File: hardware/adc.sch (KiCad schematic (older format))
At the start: 36 parts, among them U39 LP5907-3.0, U8 LTC2292

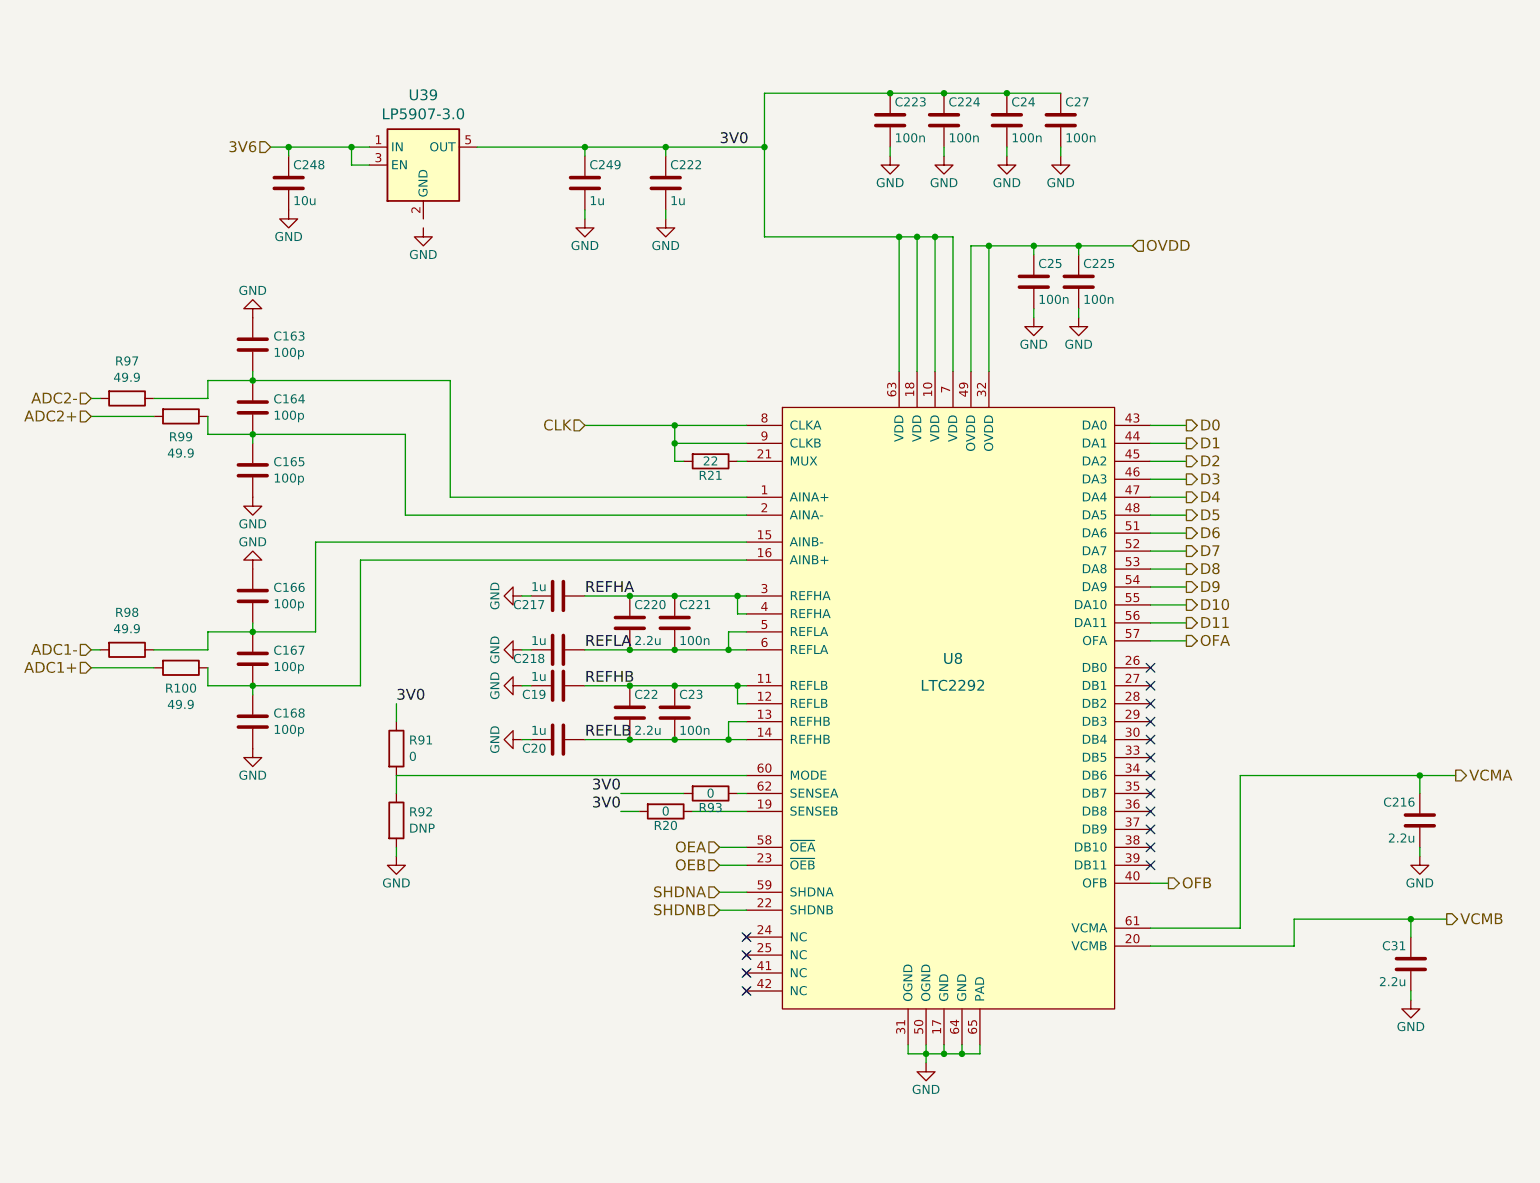
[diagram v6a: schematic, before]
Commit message: Improved documentation and parts of the schematic.
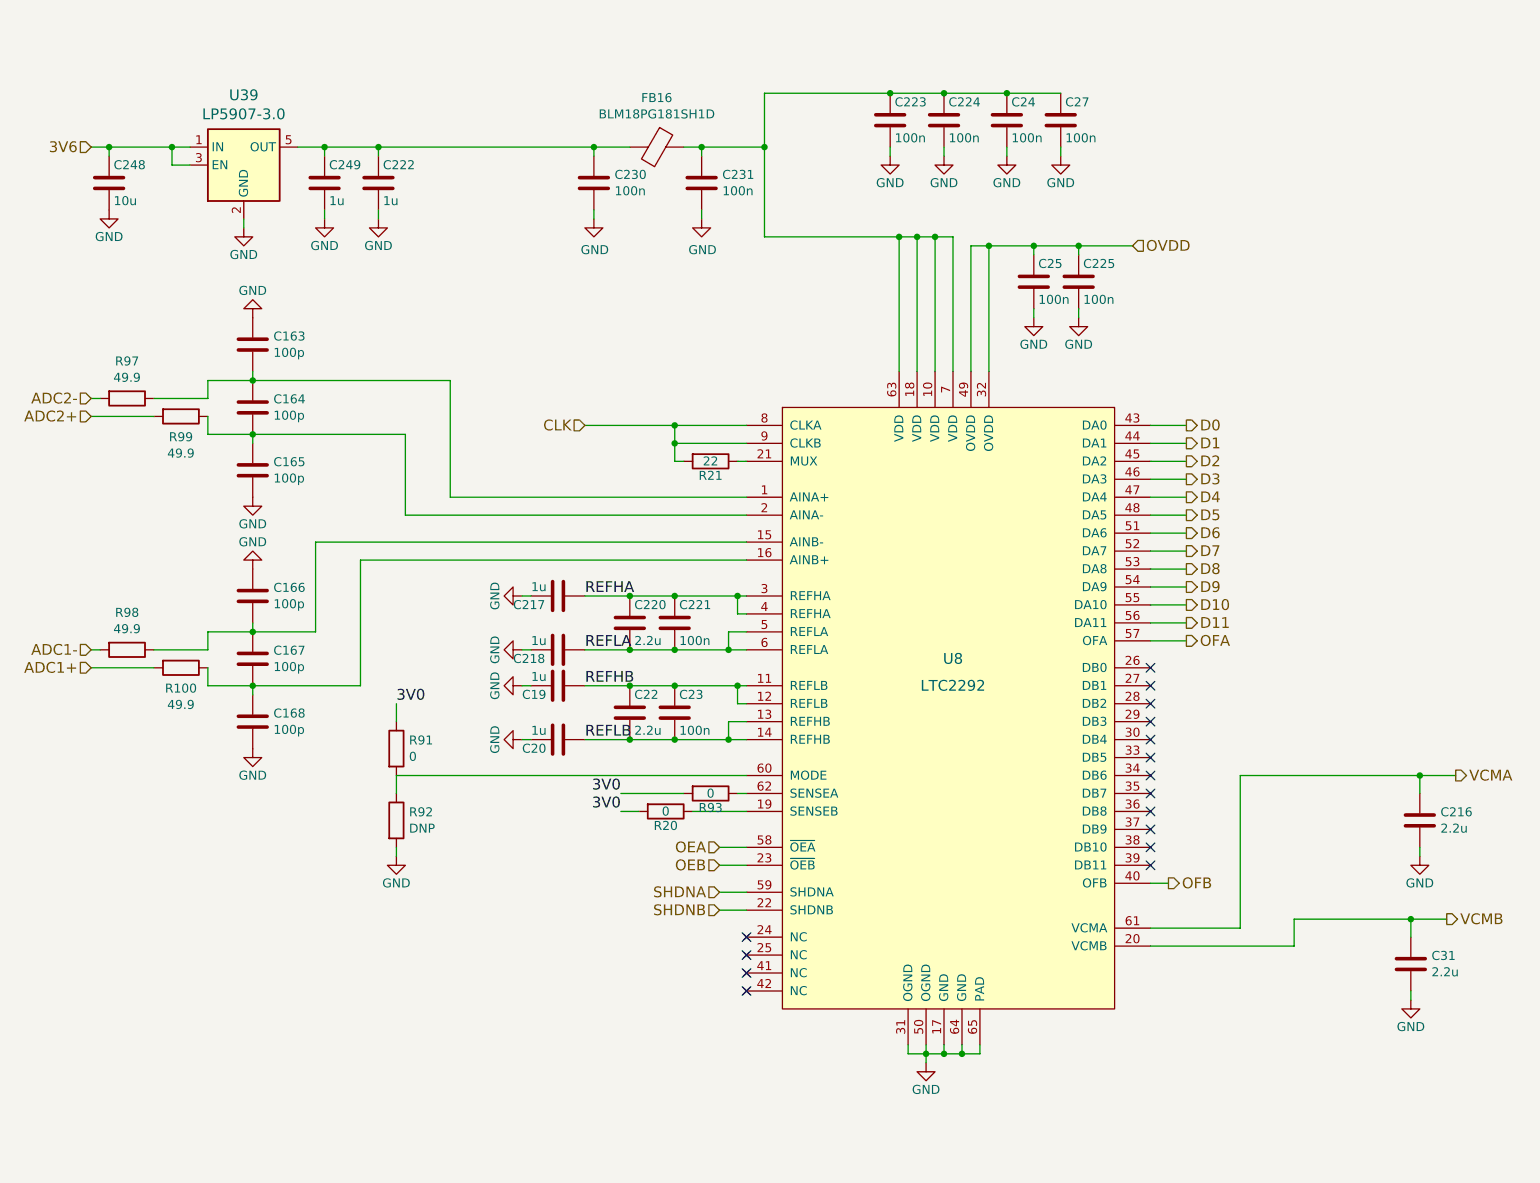
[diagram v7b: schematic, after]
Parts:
- added C230, C231: 100n, Capacitor_SMD:C_0402_1005Metric, symbol Device:C
- added FB16: BLM18PG181SH1D, Inductor_SMD:L_0603_1608Metric, symbol Device:Ferrite_Bead
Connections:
- net 3V0: no longer C222.1, C223.1, C224.1, C24.1, C249.1, C27.1, U39.5 (OUT), U8.10 (VDD), U8.18 (VDD), U8.63 (VDD), U8.7 (VDD)
- net GND: now also U39.2 (GND), C230.2, C231.2
- new net: C223.1, C224.1, C231.1, C24.1, C27.1, FB16.1, U8.10 (VDD), U8.18 (VDD), U8.63 (VDD), U8.7 (VDD)
- new net: C222.1, C230.1, C249.1, FB16.2, U39.5 (OUT)
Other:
- moved on the sheet: C222, C248, C249, U39
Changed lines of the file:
@@
 L Device:C C222
 U 1 1 583E443A
-P 4350 1550
-F 0 "C222" H 4375 1650 50  0000 L CNN
-F 1 "1u" H 4375 1450 50  0000 L CNN
-F 2 "Capacitor_SMD:C_0603_1608Metric" H 4388 1400 30  0001 C CNN
-F 3 "" H 4350 1550 60  0000 C CNN
-F 4 "CL10B105MO8NNWC" H 0   0   50  0001 C CNN "MFN"
-	1    4350 1550
+P 2750 1550
+F 0 "C222" H 2775 1650 50  0000 L CNN
+F 1 "1u" H 2775 1450 50  0000 L CNN
+F 2 "Capacitor_SMD:C_0603_1608Metric" H 2788 1400 30  0001 C CNN
+F 3 "" H 2750 1550 60  0000 C CNN
+F 4 "CL10B105MO8NNWC" H -1600 0   50  0001 C CNN "MFN"
+	1    2750 1550
 	1    0    0    -1
 $EndComp
@@
 L power:GND #PWR061
 U 1 1 583E44F5
-P 4350 1750
-F 0 "#PWR061" H 4350 1500 50  0001 C CNN
-F 1 "GND" H 4350 1600 50  0000 C CNN
-F 2 "" H 4350 1750 60  0000 C CNN
-F 3 "" H 4350 1750 60  0000 C CNN
-	1    4350 1750
+P 2750 1750
+F 0 "#PWR061" H 2750 1500 50  0001 C CNN
+F 1 "GND" H 2750 1600 50  0000 C CNN
+F 2 "" H 2750 1750 60  0000 C CNN
+F 3 "" H 2750 1750 60  0000 C CNN
+	1    2750 1750
 	1    0    0    -1
 $EndComp
@@
 U 1 1 583E8D35
 P 8550 5100
-F 0 "C216" H 8575 5200 50  0000 L CNN
-F 1 "2.2u" H 8575 5000 50  0000 L CNN
+F 0 "C216" H 8435 5146 50  0000 R CNN
+F 1 "2.2u" H 8435 5055 50  0000 R CNN
 F 2 "Capacitor_SMD:C_0603_1608Metric" H 8588 4950 30  0001 C CNN
 F 3 "" H 8550 5100 60  0000 C CNN
@@
 Text Label 2850 4450 0    60   ~ 0
 3V0
-Text Label 4650 1350 0    60   ~ 0
-3V0
 Text HLabel 7250 4100 2    60   Output ~ 0
 OFA
@@
 	2900 3400 4800 3400
 Wire Wire Line
-	3300 1350 3900 1350
-Wire Wire Line
-	4900 1050 4900 1350
-Wire Wire Line
-	4350 1400 4350 1350
-Connection ~ 4350 1350
-Wire Wire Line
-	4350 1700 4350 1750
+	2300 1350 2450 1350
+Wire Wire Line
+	2750 1400 2750 1350
+Wire Wire Line
+	2750 1700 2750 1750
 Wire Wire Line
 	5900 1350 5900 1400
@@
 L Regulator_Linear:LP5907MFX-3.0 U39
 U 1 1 58526584
-P 3000 1450
-F 0 "U39" H 3000 1839 60  0000 C CNN
-F 1 "LP5907-3.0" H 3000 1733 60  0000 C CNN
-F 2 "Package_TO_SOT_SMD:SOT-23-5" H 3000 1500 60  0001 C CNN
-F 3 "" H 3000 1500 60  0000 C CNN
-F 4 "LP5907MFX-3.0/NOPB" H 200 50  50  0001 C CNN "MFN"
-	1    3000 1450
+P 2000 1450
+F 0 "U39" H 2000 1839 60  0000 C CNN
+F 1 "LP5907-3.0" H 2000 1733 60  0000 C CNN
+F 2 "Package_TO_SOT_SMD:SOT-23-5" H 2000 1500 60  0001 C CNN
+F 3 "" H 2000 1500 60  0000 C CNN
+F 4 "LP5907MFX-3.0/NOPB" H -800 50  50  0001 C CNN "MFN"
+	1    2000 1450
 	1    0    0    -1
 $EndComp
@@
 L power:GND #PWR071
 U 1 1 585266D4
-P 3000 1800
-F 0 "#PWR071" H 3000 1550 50  0001 C CNN
-F 1 "GND" H 3000 1650 50  0000 C CNN
-F 2 "" H 3000 1800 60  0000 C CNN
-F 3 "" H 3000 1800 60  0000 C CNN
-	1    3000 1800
-	1    0    0    -1
-$EndComp
-Wire Wire Line
-	2700 1450 2600 1450
-Wire Wire Line
-	2600 1450 2600 1350
-Wire Wire Line
-	2150 1350 2250 1350
+P 2000 1800
+F 0 "#PWR071" H 2000 1550 50  0001 C CNN
+F 1 "GND" H 2000 1650 50  0000 C CNN
+F 2 "" H 2000 1800 60  0000 C CNN
+F 3 "" H 2000 1800 60  0000 C CNN
+	1    2000 1800
+	1    0    0    -1
+$EndComp
+Wire Wire Line
+	1700 1450 1600 1450
+Wire Wire Line
+	1600 1450 1600 1350
+Wire Wire Line
+	1150 1350 1250 1350
 $Comp
 L Device:C C248
 U 1 1 5852675F
-P 2250 1550
-F 0 "C248" H 2275 1650 50  0000 L CNN
-F 1 "10u" H 2275 1450 50  0000 L CNN
-F 2 "Capacitor_SMD:C_0805_2012Metric" H 2288 1400 30  0001 C CNN
-F 3 "" H 2250 1550 60  0000 C CNN
-F 4 "CL21B106KQQNNNE" H 400 0   50  0001 C CNN "MFN"
-	1    2250 1550
+P 1250 1550
+F 0 "C248" H 1275 1650 50  0000 L CNN
+F 1 "10u" H 1275 1450 50  0000 L CNN
+F 2 "Capacitor_SMD:C_0805_2012Metric" H 1288 1400 30  0001 C CNN
+F 3 "" H 1250 1550 60  0000 C CNN
+F 4 "CL21B106KQQNNNE" H -600 0   50  0001 C CNN "MFN"
+	1    1250 1550
 	1    0    0    -1
 $EndComp
@@
 L power:GND #PWR072
 U 1 1 585267C4
-P 2250 1700
-F 0 "#PWR072" H 2250 1450 50  0001 C CNN
-F 1 "GND" H 2250 1550 50  0000 C CNN
-F 2 "" H 2250 1700 60  0000 C CNN
-F 3 "" H 2250 1700 60  0000 C CNN
-	1    2250 1700
-	1    0    0    -1
-$EndComp
-Wire Wire Line
-	2250 1400 2250 1350
-Connection ~ 2600 1350
-Connection ~ 2250 1350
-Text HLabel 2150 1350 0    60   Input ~ 0
+P 1250 1700
+F 0 "#PWR072" H 1250 1450 50  0001 C CNN
+F 1 "GND" H 1250 1550 50  0000 C CNN
+F 2 "" H 1250 1700 60  0000 C CNN
+F 3 "" H 1250 1700 60  0000 C CNN
+	1    1250 1700
+	1    0    0    -1
+$EndComp
+Wire Wire Line
+	1250 1400 1250 1350
+Connection ~ 1600 1350
+Connection ~ 1250 1350
+Text HLabel 1150 1350 0    60   Input ~ 0
 3V6
 $Comp
 L Device:C C249
 U 1 1 585275B5
-P 3900 1550
-F 0 "C249" H 3925 1650 50  0000 L CNN
-F 1 "1u" H 3925 1450 50  0000 L CNN
-F 2 "Capacitor_SMD:C_0603_1608Metric" H 3938 1400 30  0001 C CNN
-F 3 "" H 3900 1550 60  0000 C CNN
-F 4 "CL10B105MO8NNWC" H 0   0   50  0001 C CNN "MFN"
-	1    3900 1550
+P 2450 1550
+F 0 "C249" H 2475 1650 50  0000 L CNN
+F 1 "1u" H 2475 1450 50  0000 L CNN
+F 2 "Capacitor_SMD:C_0603_1608Metric" H 2488 1400 30  0001 C CNN
+F 3 "" H 2450 1550 60  0000 C CNN
+F 4 "CL10B105MO8NNWC" H -1450 0   50  0001 C CNN "MFN"
+	1    2450 1550
 	1    0    0    -1
 $EndComp
@@
 L power:GND #PWR073
 U 1 1 58527606
-P 3900 1750
-F 0 "#PWR073" H 3900 1500 50  0001 C CNN
-F 1 "GND" H 3900 1600 50  0000 C CNN
-F 2 "" H 3900 1750 60  0000 C CNN
-F 3 "" H 3900 1750 60  0000 C CNN
-	1    3900 1750
-	1    0    0    -1
-$EndComp
-Wire Wire Line
-	3900 1750 3900 1700
-Wire Wire Line
-	3900 1400 3900 1350
-Connection ~ 3900 1350
+P 2450 1750
+F 0 "#PWR073" H 2450 1500 50  0001 C CNN
+F 1 "GND" H 2450 1600 50  0000 C CNN
+F 2 "" H 2450 1750 60  0000 C CNN
+F 3 "" H 2450 1750 60  0000 C CNN
+	1    2450 1750
+	1    0    0    -1
+$EndComp
+Wire Wire Line
+	2450 1750 2450 1700
+Wire Wire Line
+	2450 1400 2450 1350
 Text Label 3900 3850 0    60   ~ 0
 REFHA
@@
 Connection ~ 6250 1050
 Connection ~ 5900 1050
-Connection ~ 4900 1350
 Connection ~ 5600 1050
 Wire Wire Line
@@
 U 1 1 5943E130
 P 8500 5900
-F 0 "C31" H 8525 6000 50  0000 L CNN
-F 1 "2.2u" H 8525 5800 50  0000 L CNN
+F 0 "C31" H 8385 5946 50  0000 R CNN
+F 1 "2.2u" H 8385 5855 50  0000 R CNN
 F 2 "Capacitor_SMD:C_0603_1608Metric" H 8538 5750 30  0001 C CNN
 F 3 "" H 8500 5900 60  0000 C CNN
@@
 Connection ~ 2050 4350
 Wire Wire Line
-	4350 1350 4900 1350
-Wire Wire Line
 	5800 6400 5800 6450
 Wire Wire Line
@@
 	8550 4850 8750 4850
 Wire Wire Line
-	2600 1350 2700 1350
-Wire Wire Line
-	2250 1350 2600 1350
-Wire Wire Line
-	3900 1350 4350 1350
+	1600 1350 1700 1350
+Wire Wire Line
+	1250 1350 1600 1350
 Wire Wire Line
 	5900 6400 6000 6400
@@
 	5900 1050 6250 1050
 Wire Wire Line
+	5600 1050 5900 1050
+Wire Wire Line
+	6150 1900 6400 1900
+Wire Wire Line
+	6400 1900 6650 1900
+Wire Wire Line
+	8500 5650 8700 5650
+Wire Wire Line
+	2050 2650 3150 2650
+Wire Wire Line
+	2050 2950 2900 2950
+Wire Wire Line
+	2050 4050 2400 4050
+Wire Wire Line
+	2050 4350 2650 4350
+Wire Wire Line
+	7550 4850 8550 4850
+Wire Wire Line
+	7850 5650 8500 5650
+Wire Wire Line
+	2000 1800 2000 1750
+Connection ~ 2450 1350
+Wire Wire Line
+	2450 1350 2750 1350
+Connection ~ 2750 1350
+Wire Wire Line
+	4900 1050 4900 1350
+$Comp
+L Device:Ferrite_Bead FB?
+U 1 1 5D83CEED
+P 4300 1350
+AR Path="/5D83CEED" Ref="FB?"  Part="1"
+AR Path="/59395D6A/583E250D/5D83CEED" Ref="FB16"  Part="1"
+F 0 "FB16" V 4026 1350 50  0000 C CNN
+F 1 "BLM18PG181SH1D" V 4117 1350 50  0000 C CNN
+F 2 "Inductor_SMD:L_0603_1608Metric" H 4300 1350 60  0001 C CNN
+F 3 "https://www.murata.com/en-us/products/productdata/8796738650142/ENFA0003.pdf" H 4300 1350 60  0001 C CNN
+F 4 "BLM18PG181SH1D" H -50 -3950 50  0001 C CNN "MFN"
+	1    4300 1350
+	0    1    1    0
+$EndComp
+Wire Wire Line
+	2750 1350 3950 1350
+Wire Wire Line
+	4450 1350 4550 1350
+Connection ~ 4900 1350
+Wire Wire Line
 	4900 1350 4900 1850
-Wire Wire Line
-	5600 1050 5900 1050
-Wire Wire Line
-	6150 1900 6400 1900
-Wire Wire Line
-	6400 1900 6650 1900
-Wire Wire Line
-	8500 5650 8700 5650
-Wire Wire Line
-	2050 2650 3150 2650
-Wire Wire Line
-	2050 2950 2900 2950
-Wire Wire Line
-	2050 4050 2400 4050
-Wire Wire Line
-	2050 4350 2650 4350
-Wire Wire Line
-	7550 4850 8550 4850
-Wire Wire Line
-	7850 5650 8500 5650
+$Comp
+L Device:C C231
+U 1 1 5D84B592
+P 4550 1550
+F 0 "C231" H 4665 1596 50  0000 L CNN
+F 1 "100n" H 4665 1505 50  0000 L CNN
+F 2 "Capacitor_SMD:C_0402_1005Metric" H 4588 1400 30  0001 C CNN
+F 3 "" H 4550 1550 60  0000 C CNN
+F 4 "CL05B104KO5NNNC" H -1050 350 50  0001 C CNN "MFN"
+	1    4550 1550
+	1    0    0    -1
+$EndComp
+Wire Wire Line
+	4550 1400 4550 1350
+Connection ~ 4550 1350
+Wire Wire Line
+	4550 1350 4900 1350
+$Comp
+L power:GND #PWR0268
+U 1 1 5D852C8A
+P 4550 1750
+F 0 "#PWR0268" H 4550 1500 50  0001 C CNN
+F 1 "GND" H 4555 1577 50  0000 C CNN
+F 2 "" H 4550 1750 50  0001 C CNN
+F 3 "" H 4550 1750 50  0001 C CNN
+	1    4550 1750
+	1    0    0    -1
+$EndComp
+Wire Wire Line
+	4550 1750 4550 1700
+$Comp
+L Device:C C230
+U 1 1 5D85A49D
+P 3950 1550
+F 0 "C230" H 4065 1596 50  0000 L CNN
+F 1 "100n" H 4065 1505 50  0000 L CNN
+F 2 "Capacitor_SMD:C_0402_1005Metric" H 3988 1400 30  0001 C CNN
+F 3 "" H 3950 1550 60  0000 C CNN
+F 4 "CL05B104KO5NNNC" H -1650 350 50  0001 C CNN "MFN"
+	1    3950 1550
+	1    0    0    -1
+$EndComp
+Wire Wire Line
+	3950 1400 3950 1350
+Connection ~ 3950 1350
+Wire Wire Line
+	3950 1350 4150 1350
+$Comp
+L power:GND #PWR0267
+U 1 1 5D861E18
+P 3950 1750
+F 0 "#PWR0267" H 3950 1500 50  0001 C CNN
+F 1 "GND" H 3955 1577 50  0000 C CNN
+F 2 "" H 3950 1750 50  0001 C CNN
+F 3 "" H 3950 1750 50  0001 C CNN
+	1    3950 1750
+	1    0    0    -1
+$EndComp
+Wire Wire Line
+	3950 1750 3950 1700
 $EndSCHEMATC

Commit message: Changed components to official libs.
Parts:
- U8: footprint Package_DFN_QFN:QFN-64-1EP_9x9mm_P0.5mm_EP4.85x4.85mm -> Package_DFN_QFN:QFN-64-1EP_9x9mm_P0.5mm_EP7.15x7.15mm; symbol fmcw-rescue:LTC229X-fmcw3-rescue -> Analog_ADC:LTC2292xUP
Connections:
- net GND: now also C216.1; no longer C216.2
- net SHDNA: now also U8.22 (SHDNB); no longer U8.59 (SHDNA)
- net SHDNB: now also U8.59 (SHDNA); no longer U8.22 (SHDNB)
- net VCMA: now also C216.2; no longer C216.1
- net at C166.2, C167.1, R98.1: now also U8.16 (AINB+); no longer U8.15 (AINB-)
- net at C167.2, C168.1, R100.1: now also U8.15 (AINB-); no longer U8.16 (AINB+)
- net REFHA: no longer names the net of C217.1, C220.1, C221.1, U8.3 (REFHA), U8.4 (REFHA)
- net REFHB: no longer names the net of C19.1, C22.1, C23.1
- net REFHB: now also U8.13 (REFHB), U8.14 (REFHB); no longer U8.11 (REFLB), U8.12 (REFLB)
- net REFLA: no longer names the net of C218.1, C220.2, C221.2, U8.5 (REFLA), U8.6 (REFLA)
- net REFLB: no longer names the net of C20.1, C22.2, C23.2
- net REFLB: now also U8.11 (REFLB), U8.12 (REFLB); no longer U8.13 (REFHB), U8.14 (REFHB)
- no-connect marks 16 -> 12
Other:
- moved on the sheet: C163, C164, C165, C166, C167, C168, C19, C20, C216, C217, C218, C22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
